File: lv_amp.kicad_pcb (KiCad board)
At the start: 2 copper layers, 139.7 x 88.9 mm, 80 parts, among them J1 AudioJack2, J2 Jack-DC, J3 AudioJack2, Q1 Q_NMOS_DGS, U1 ECC83, U2 TL072, U3 ECC83, U4 ECC83, U5 MAX1771xSA

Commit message: initial layout
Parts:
- C12, C16, C18, C21, C23, C4, C6, C9, J1, J2, J3, RV1, RV2, RV3, RV4, TP1, TP2, TP3, TP4, TP5, TP6, TP7, TP8, TP9, U1, U3, U4: moved to B.Cu
- moved J3 190.2 mm to (159.8, 99.8)
- moved RV3 179.7 mm to (158.8, 137.0), turned to -90 degrees
- moved J1 171.7 mm to (47.5, 121.5), turned to -90 degrees
- moved TP1 165.9 mm to (62.0, 99.0), turned to 180 degrees
- moved C6 155.7 mm to (73.0, 123.0)
- moved R5 155.1 mm to (167.0, 108.0)
- moved C4 152.7 mm to (157.5, 120.0)
- moved RV2 149.8 mm to (108.0, 136.8), turned to -90 degrees
- moved RV1 149.3 mm to (133.3, 137.0), turned to -90 degrees
- moved R4 147.7 mm to (48.8, 113.2), turned to 180 degrees
- moved C9 146.2 mm to (172.5, 108.0), turned to 180 degrees
- moved C3 146.0 mm to (154.0, 132.0), turned to -90 degrees
- moved C10 145.5 mm to (80.0, 104.0), turned to 180 degrees
- moved R9 141.4 mm to (165.0, 120.0)
- moved R22 140.3 mm to (114.0, 100.0)
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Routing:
- net +12V: track 31.6 -> 315.1 mm
- net HT: track 47.6 -> 162.6 mm
- net Net-(C2-Pad1): track 0.00 -> 63.9 mm
- net Net-(C1-Pad2): track 0.00 -> 58.4 mm
- net /u3ap: track 0.00 -> 47.4 mm
- net Net-(RV2-Pad2): track 0.00 -> 47.0 mm
- net Net-(R11-Pad2): track 0.00 -> 42.1 mm
- net Net-(C4-Pad1): track 0.00 -> 36.2 mm
- net Net-(C2-Pad2): track 0.00 -> 30.9 mm
- net Net-(C9-Pad1): track 0.00 -> 27.6 mm
- net /u4ap: track 0.00 -> 26.0 mm
- net Net-(R4-Pad1): track 0.00 -> 21.8 mm
- net /u3bp: track 0.00 -> 21.5 mm
- net Net-(C10-Pad1): track 0.00 -> 17.1 mm
- net Net-(C6-Pad2): track 0.00 -> 17.1 mm
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
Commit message: tighter layout
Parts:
- removed TP1, TP5, TP6, TP7, TP8: TestPoint, TestPoint:TestPoint_THTPad_2.0x2.0mm_Drill1.0mm
- moved R19 39.6 mm to (122.0, 127.0), turned to 0 degrees
- moved R26 31.8 mm to (130.0, 125.0), turned to -90 degrees
- moved R28 31.4 mm to (132.0, 116.0)
- moved R27 30.4 mm to (133.0, 120.0)
- moved C6 30.3 mm to (103.0, 127.0), turned to 180 degrees
- moved R31 28.9 mm to (129.0, 75.0)
- moved C21 28.6 mm to (127.0, 127.0), turned to 90 degrees
- moved R20 24.7 mm to (122.0, 123.0)
- moved J2 18.0 mm to (155.0, 78.1)
- moved C5 16.1 mm to (63.0, 126.0)
- moved R13 16.0 mm to (73.0, 112.0)
- moved C12 15.3 mm to (94.0, 107.0), turned to -90 degrees
- moved C4 14.9 mm to (143.5, 125.1)
- moved C9 14.9 mm to (158.5, 113.1)
- moved J3 14.9 mm to (145.8, 104.9)
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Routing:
- net +12V: track 315.1 -> 0.00 mm
- net HT: track 162.6 -> 0.00 mm
- net Net-(C2-Pad1): track 63.9 -> 0.00 mm
- net Net-(C1-Pad2): track 58.4 -> 0.00 mm
- net /u3ap: track 47.4 -> 0.00 mm
- net Net-(RV2-Pad2): track 47.0 -> 0.00 mm
- net Net-(R11-Pad2): track 42.1 -> 0.00 mm
- net Net-(C4-Pad1): track 36.2 -> 0.00 mm
- net Net-(C2-Pad2): track 30.9 -> 0.00 mm
- net /d1a: track 30.2 -> 0.00 mm
- net Net-(C9-Pad1): track 27.6 -> 0.00 mm
- net /u4ap: track 26.0 -> 0.00 mm
- net Net-(R4-Pad1): track 21.8 -> 0.00 mm
- net /u3bp: track 21.5 -> 0.00 mm
- net Net-(C10-Pad1): track 17.1 -> 0.00 mm
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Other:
- board size 139.7 x 88.9 mm -> 127 x 76.2 mm

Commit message: flipsies
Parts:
- moved J2 108.0 mm to (47.0, 74.9), turned to 0 degrees
- moved C15 98.0 mm to (64.0, 113.8)
- moved C4 98.0 mm to (45.5, 124.9)
- moved C9 98.0 mm to (60.5, 112.9)
- moved R12 98.0 mm to (47.0, 108.8)
- moved R3 98.0 mm to (59.0, 117.9)
- moved R5 98.0 mm to (55.0, 112.9)
- moved R6 98.0 mm to (57.0, 124.9)
- moved R9 98.0 mm to (63.0, 118.8)
- moved U2 98.0 mm to (54.0, 118.9)
- moved L1 97.2 mm to (151.0, 87.0), turned to 90 degrees
- moved J1 97.0 mm to (144.5, 121.5)
- moved R2 97.0 mm to (146.0, 116.0)
- moved R4 97.0 mm to (146.0, 118.0)
- moved C3 96.0 mm to (58.0, 131.8)
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
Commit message: route/re-annotate
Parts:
- added H1: MountingHole_Pad, MountingHole:MountingHole_3.2mm_M3, F.Cu at (43.5, 68.0)
- added H2: MountingHole_Pad, MountingHole:MountingHole_3.2mm_M3, F.Cu at (160.0, 68.0)
- added H3: MountingHole_Pad, MountingHole:MountingHole_3.2mm_M3, F.Cu at (42.5, 134.0)
- added H4: MountingHole_Pad, MountingHole:MountingHole_3.2mm_M3, F.Cu at (161.5, 135.0)
- moved C19 30.8 mm to (111.0, 118.0), turned to 180 degrees
- moved R29 29.5 mm to (81.5, 121.0)
- moved R31 29.5 mm to (81.5, 125.0), turned to 0 degrees
- moved C3 15.4 mm to (91.0, 89.5), turned to 90 degrees
- moved R9 12.5 mm to (86.0, 89.5), turned to 90 degrees
- moved R24 8.93 mm to (139.5, 117.0)
- moved C11 8.36 mm to (138.0, 121.0)
- moved R14 7.21 mm to (102.0, 106.0)
- moved R28 6.30 mm to (88.5, 119.5), turned to 90 degrees
- moved R33 4.98 mm to (123.5, 131.5), turned to 180 degrees
- moved R16 4.03 mm to (102.0, 108.5)
- moved J1 3.12 mm to (47.0, 78.0)
- moved C21 3.04 mm to (106.0, 123.5), turned to 180 degrees
- moved RV4 3.00 mm to (60.0, 136.8)
- moved R4 2.15 mm to (76.5, 84.5), turned to 180 degrees
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- renumbered C22 to C1, C5 to C11, C7 to C12, C3 to C13, C2 to C14, C8 to C15, C23 to C16, C12 to C17, C9 to C18, C16 to C19, C1 to C2, C21 to C20, C18 to C21, C4 to C22, C6 to C23, C19 to C3, C13 to C4, C20 to C5, C11 to C6, C14 to C7, C17 to C8, C15 to C9, J2 to J1, J3 to J2, J1 to J3, R32 to R1, R21 to R10, R28 to R11, R27 to R12, R26 to R13, R15 to R14, R18 to R15, R12 to R17, R22 to R18, R7 to R19, R31 to R2, R14 to R20, R5 to R21, R4 to R22, R13 to R23, R8 to R24, R3 to R25, R2 to R26, R9 to R27, R17 to R28, R20 to R29, R30 to R3, R6 to R30, R19 to R31, R10 to R32, R11 to R33, R29 to R4, R25 to R5, R24 to R6, R1 to R7, R33 to R8, R23 to R9, RV4 to RV1, RV1 to RV3, RV3 to RV4, TP4 to TP1, TP9 to TP4, U5 to U1, U4 to U3, U3 to U4, U1 to U5
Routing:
- net +12V: track 0.00 -> 223.9 mm, vias 0 -> 1
- net HT: track 0.00 -> 197.6 mm
- net Net-(C1-Pad2): track 0.00 -> 59.1 mm, vias 0 -> 1
- net Net-(RV2-Pad2): track 0.00 -> 54.3 mm
- net Net-(C2-Pad1): track 0.00 -> 51.4 mm
- net Net-(C2-Pad2): track 0.00 -> 49.8 mm
- net Net-(C4-Pad1): track 0.00 -> 39.6 mm
- net /u1bp: track 0.00 -> 34.9 mm
- net /u3ap: track 0.00 -> 31.1 mm
- net /u1ap: track 0.00 -> 31.1 mm
- net Net-(C9-Pad1): track 0.00 -> 30.0 mm
- net /d1a: track 0.00 -> 29.6 mm
- net /u4ap: track 0.00 -> 23.9 mm
- net /u3bg: track 0.00 -> 23.3 mm
- net /u3bp: track 0.00 -> 20.8 mm
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
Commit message: tweaks
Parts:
- renumbered C23 to C21, C21 to C22, C22 to C23, R11 to R10, R10 to R11, R17 to R15, R18 to R16, R15 to R17, R16 to R18, R20 to R19, R19 to R20, R23 to R22, R24 to R23, R22 to R24, R27 to R26, R29 to R27, R26 to R29, R7 to R4, R8 to R5, R4 to R6, R5 to R7, R6 to R8
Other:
- board text added: "lv-amp alpha0"

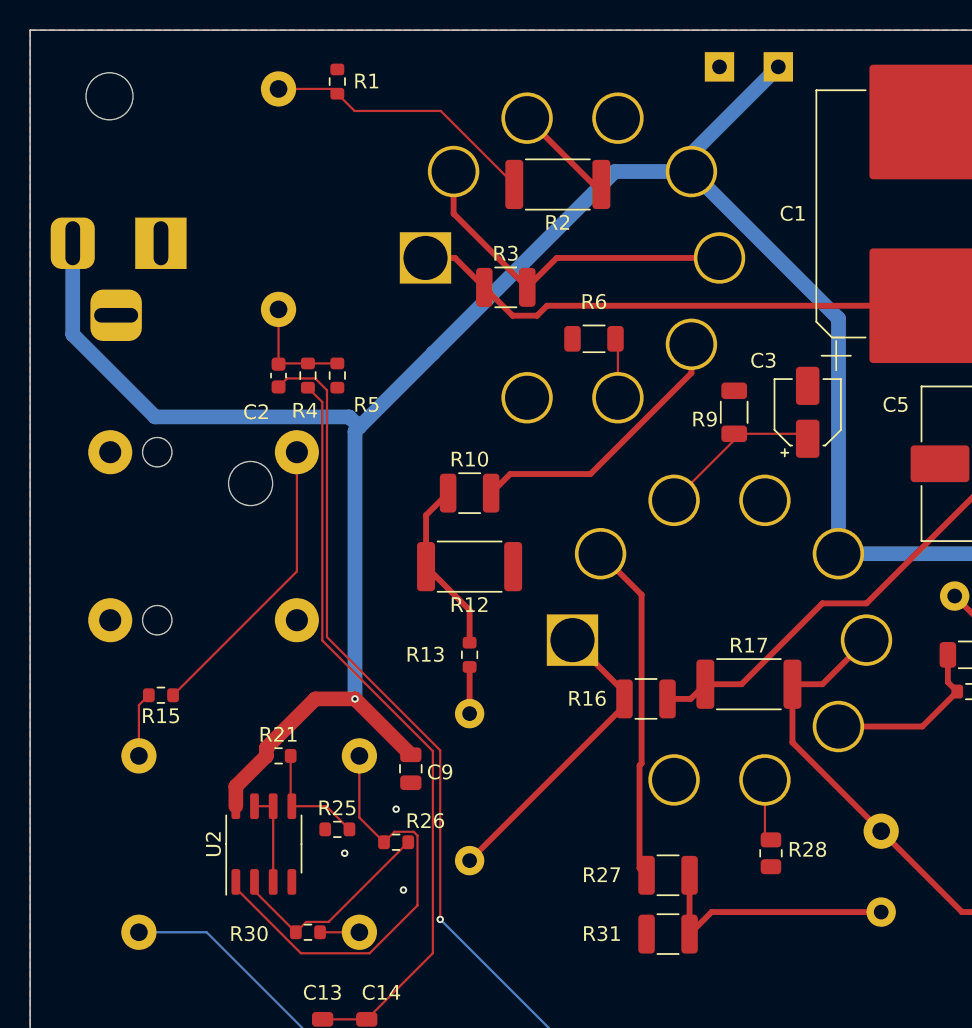
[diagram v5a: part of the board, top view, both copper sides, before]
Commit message: alpha0 errata: DC jack
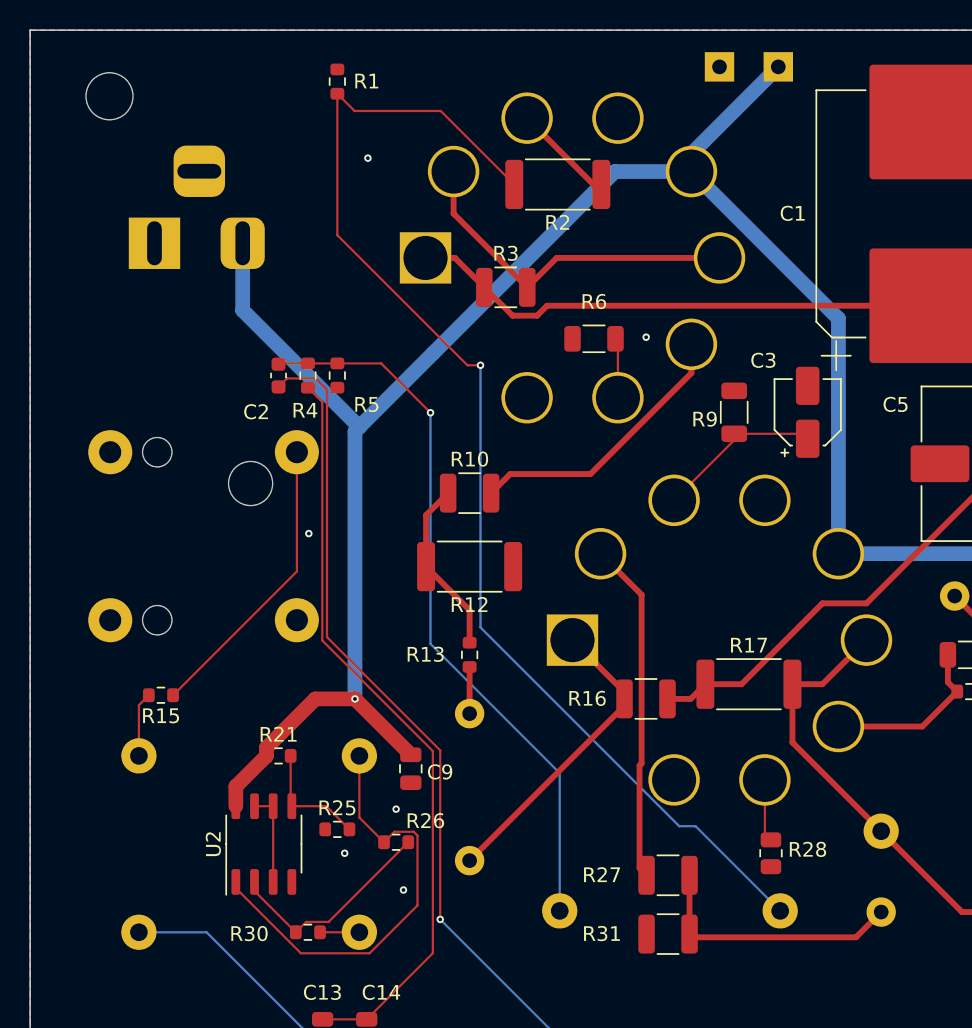
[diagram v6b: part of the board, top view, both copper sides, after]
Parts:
- moved C16 65.5 mm to (89.1, 123.4), turned to 180 degrees
- moved J1 5.56 mm to (52.6, 78.0), turned to 180 degrees
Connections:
- J1 pad 1: GND -> +12V
- J1 pad 2: +12V -> GND
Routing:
- net Net-(C16-Pad1): track 18.7 -> 83.8 mm, vias 0 -> 1
- net /tonestack: track 7.75 -> 49.3 mm, vias 0 -> 1
- net +12V: track 223.9 -> 211.4 mm
- net GND: vias 7 -> 10

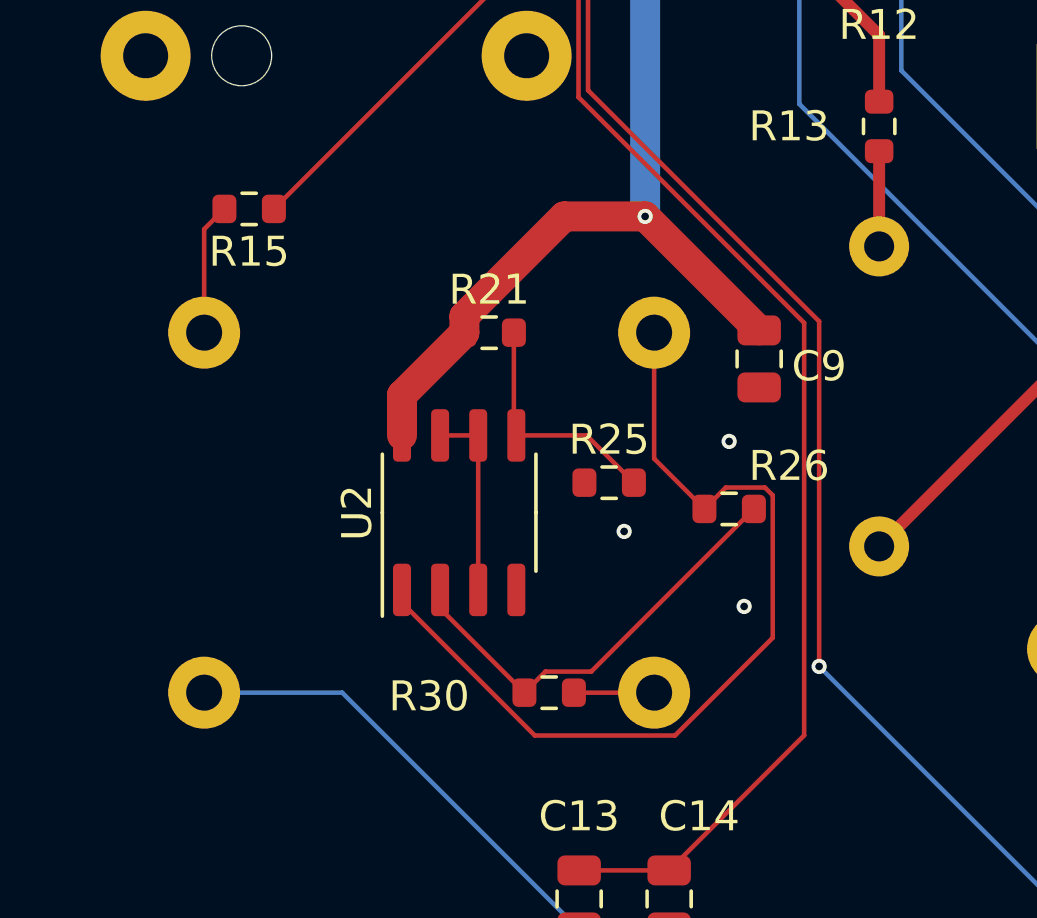
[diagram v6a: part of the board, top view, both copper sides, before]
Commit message: alpha0 errata: dd zener diode to output reference
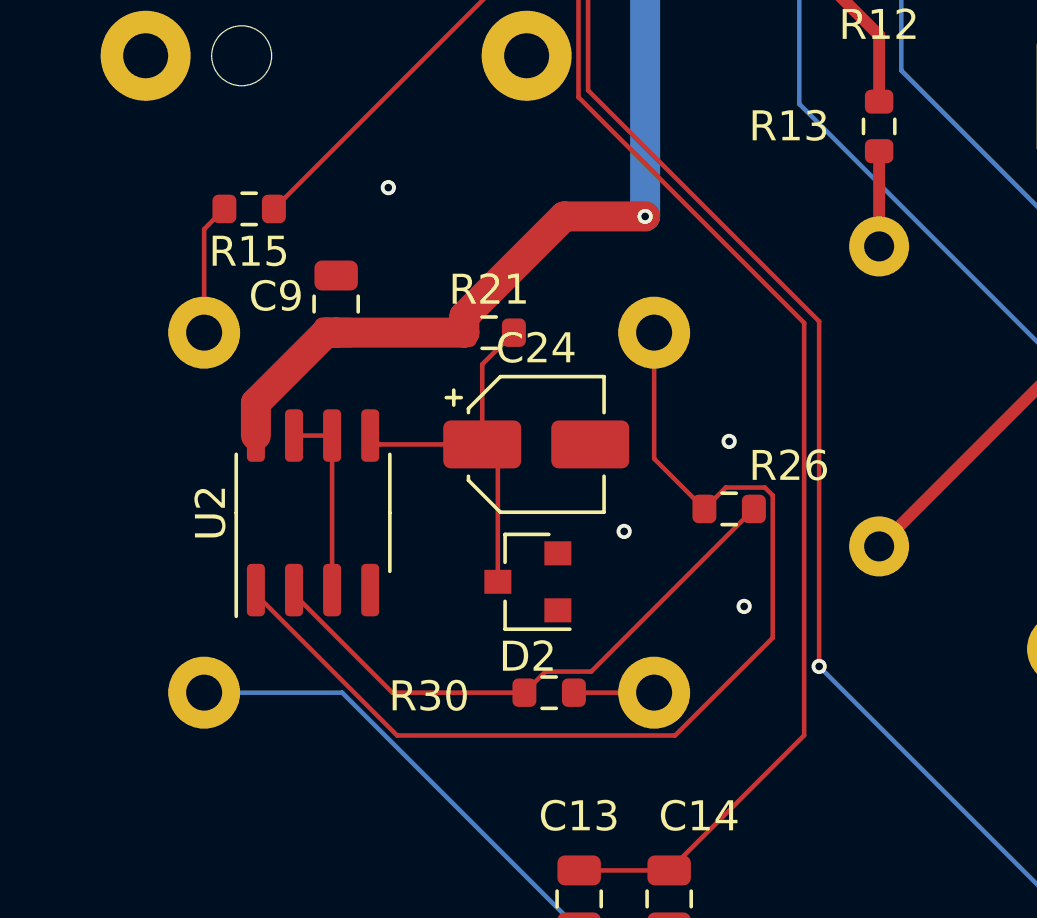
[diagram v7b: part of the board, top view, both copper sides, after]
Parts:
- removed R25: 100k, Resistor_SMD:R_0603_1608Metric
- added C24: 1uF, Capacitor_SMD:CP_Elec_4x5.4, F.Cu at (56.6, 116.6)
- added D2: Zener 3.3V, Diode_SMD:D_SOT-23_ANK, F.Cu at (56.3, 121.2)
- R21: value 100k -> 1k
- moved C9 14.2 mm to (49.9, 111.9), turned to 90 degrees
- moved U2 4.87 mm to (49.1, 118.9)
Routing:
- net Net-(R21-Pad2): track 8.03 -> 12.8 mm
- net Net-(C18-Pad1): track 30.0 -> 34.7 mm
- net Net-(R26-Pad2): track 14.8 -> 19.4 mm
- net +12V: track 211.4 -> 210.7 mm
- net GND: vias 10 -> 11

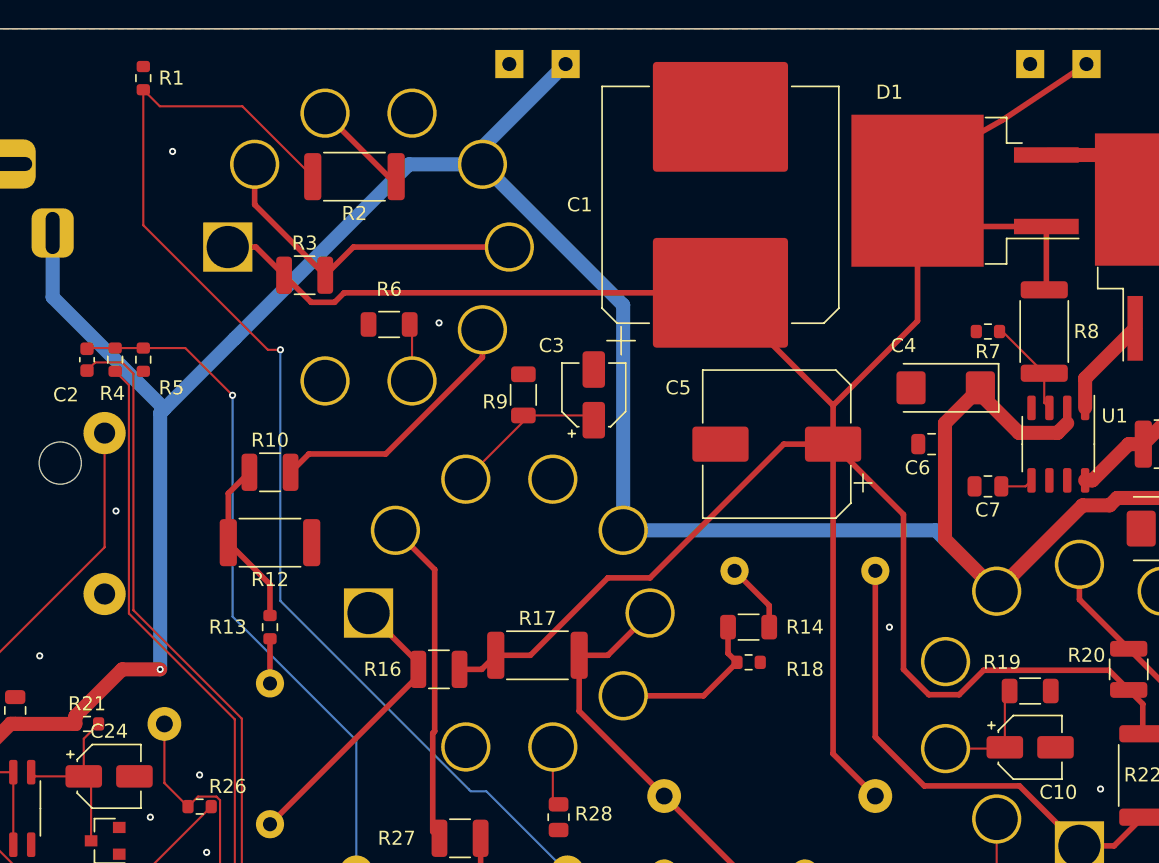
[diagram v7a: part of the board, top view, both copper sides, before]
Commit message: alpha0 errata: better output filtering on supply
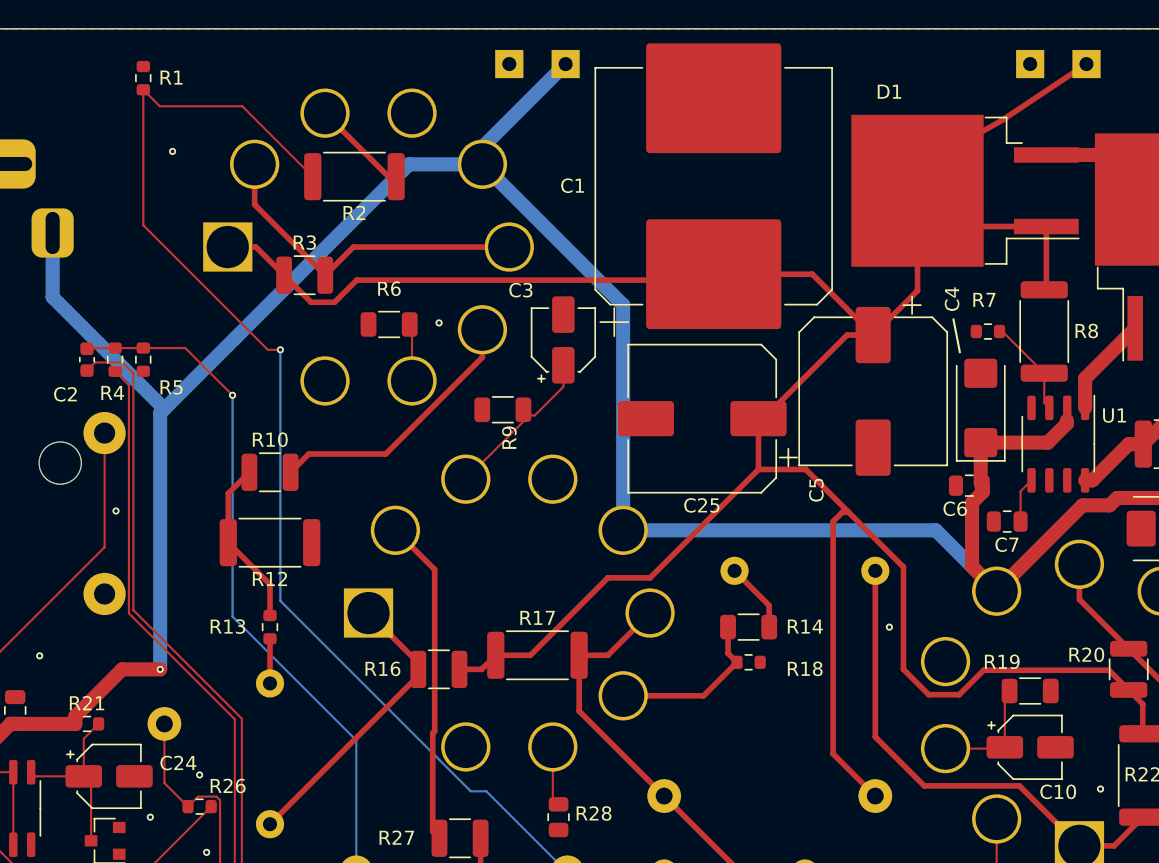
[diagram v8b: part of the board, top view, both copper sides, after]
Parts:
- added C25: 4.7uF, Capacitor_SMD:CP_Elec_10x10, F.Cu at (98.7, 91.2)
- moved C5 7.81 mm to (110.8, 89.2), turned to -90 degrees
- moved C3 4.46 mm to (88.8, 85.6)
- moved C6 3.99 mm to (117.7, 96.0)
- moved C4 2.87 mm to (118.5, 90.4), turned to 90 degrees
- moved C7 2.85 mm to (120.4, 98.5)
- moved R9 1.80 mm to (84.5, 90.6), turned to 180 degrees
- moved C1 1.40 mm to (99.5, 74.7)
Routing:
- net +12V: track 210.7 -> 204.2 mm
- net Net-(C7-Pad1): track 2.32 -> 3.25 mm
